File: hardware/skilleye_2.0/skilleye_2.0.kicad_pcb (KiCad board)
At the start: 2 copper layers, 4 parts, among them J1 TP4056 Breakout, U1 XIAO-ESP32-C6-SMD, U2 GY-521

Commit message: added 2.0 pcb layout
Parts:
- added G***: LOGO, LOGO, B.Cu at (156.0, 83.5)
- added SW1: SW_SPDT, Button_Switch_THT:SW_Slide_SPDT_Straight_CK_OS102011MS2Q, F.Cu at (144.0, 101.3)
- BT1, J1, U2: moved to B.Cu
- moved BT1 27.5 mm to (125.5, 99.3), turned to 90 degrees
- moved U1 22.9 mm to (136.4, 108.1), turned to 90 degrees
- moved U2 15.9 mm to (155.8, 99.3)
- moved J1 15.8 mm to (128.0, 99.3)
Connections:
- net Net-(BT1-+) renamed /BATT+
- net Net-(BT1--) renamed /BATT-
- J1 pad 5: Net-(J1-OUT+) -> /VBAT_RAW
- U1 pad 1: unconnected-(U1-D0-Pad1) -> /IMU_INT
- U1 pad 23: Net-(J1-OUT+) -> /VBAT_SW
- U2 pad INT: unconnected-(U2-PadINT) -> /IMU_INT
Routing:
- net /IMU_INT: track 0.00 -> 40.0 mm, vias 0 -> 1
- net +3V3: track 0.00 -> 37.4 mm, vias 0 -> 1
- net /SDA: track 0.00 -> 30.0 mm, vias 0 -> 1
- net /SCL: track 0.00 -> 22.7 mm, vias 0 -> 1
- net /BATT+: track 0.00 -> 16.6 mm
- net /BATT-: track 0.00 -> 16.6 mm
- net /VBAT_SW: track 0.00 -> 12.7 mm, vias 0 -> 1
- net /VBAT_RAW: track 0.00 -> 11.3 mm, vias 0 -> 1
- net GND: track 0.00 -> 4.80 mm, vias 0 -> 3
- added copper zone on B.Cu, net GND
- added copper zone on F.Cu, net GND
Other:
- board outline added: 52 x 74.8 mm
- board text added: "Antenna"
- board text added: "B+"
- board text added: "B-"
- board text added: "CHARGE"
- board text added: "PROG"
- board text added: "SkillEye"
- board text added: "TEAM: Purit • Rizal • Rachel • Jeslin • YuChing"
- board text added: "https://github.com/rizalfanex/SkillEye"

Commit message: update finalized PCB design
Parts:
- added G***: LOGO, LOGO, B.Cu at (155.5, 117.0)
- added G***: LOGO, LOGO, B.Cu at (155.5, 112.5)
- moved J1 0.25 mm to (128.0, 99.0)
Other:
- board text added: "WayWayWay"

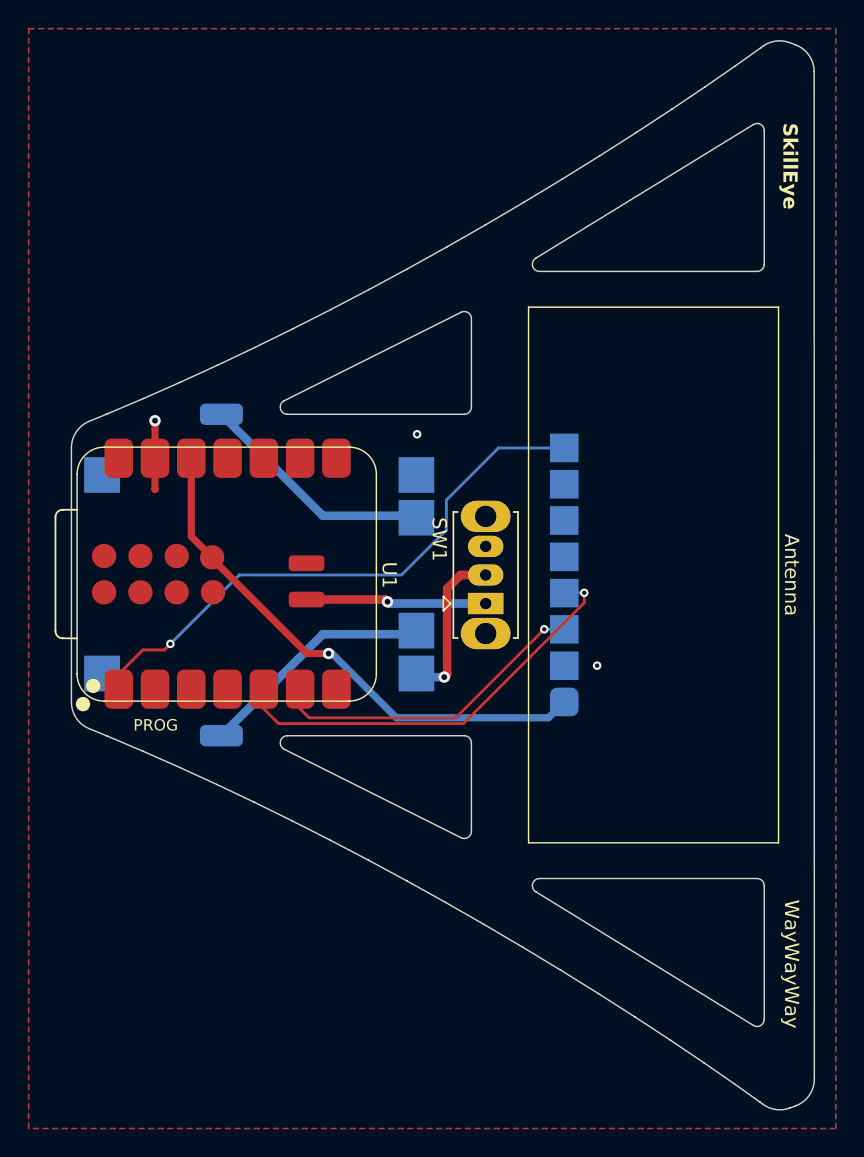
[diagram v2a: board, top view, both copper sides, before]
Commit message: layout update for fabrication constraints
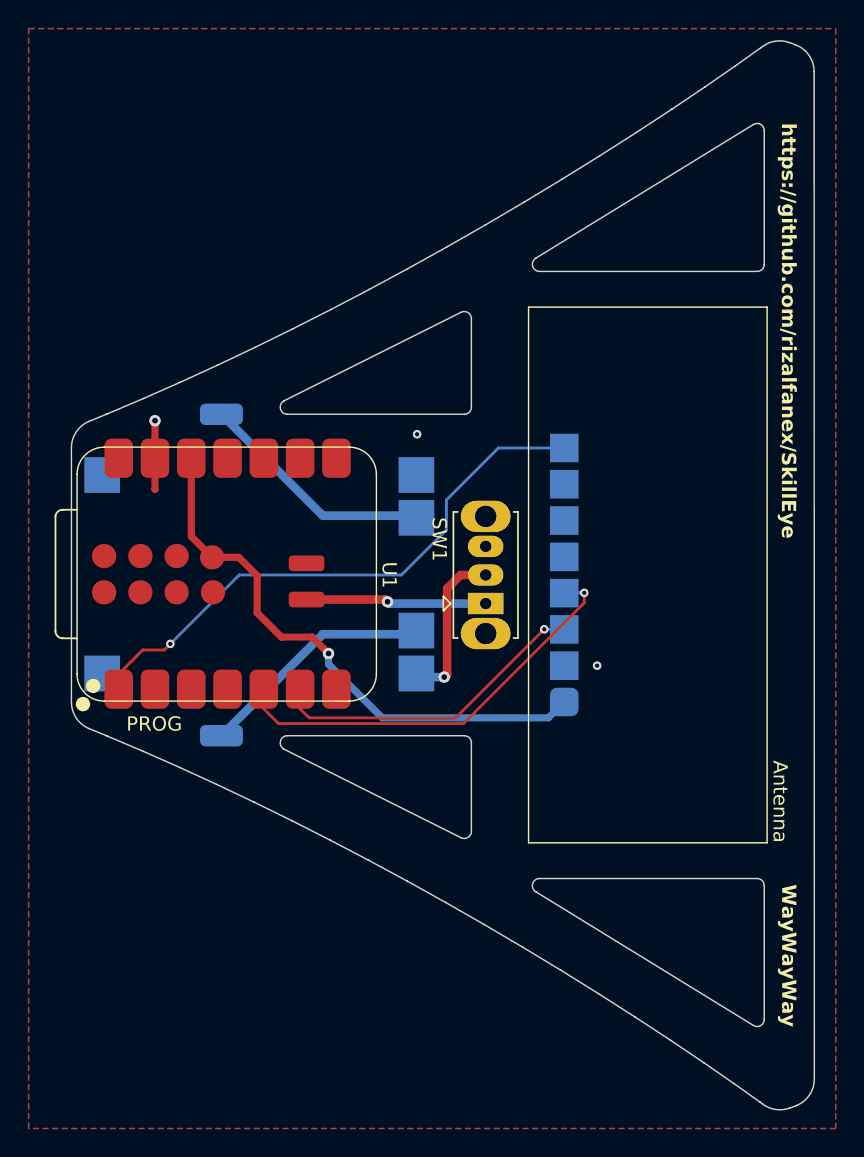
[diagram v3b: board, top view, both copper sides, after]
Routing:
- net +3V3: track 37.4 -> 39.3 mm
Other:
- board text added: "CHRG"
- board text removed: "CHARGE"
